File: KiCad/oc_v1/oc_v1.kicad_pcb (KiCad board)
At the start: 2 copper layers, 20 parts, among them J1 ESC_CTRL, J10 STPR_CTRL, J11 ENC_A, J12 ENC_A, J13 MOTOR, J14 Screw_Terminal_01x02, J2 ESC_SEN, J3 BLDC_SEN, J4 ESC_CTRL, J5 ESC_SEN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

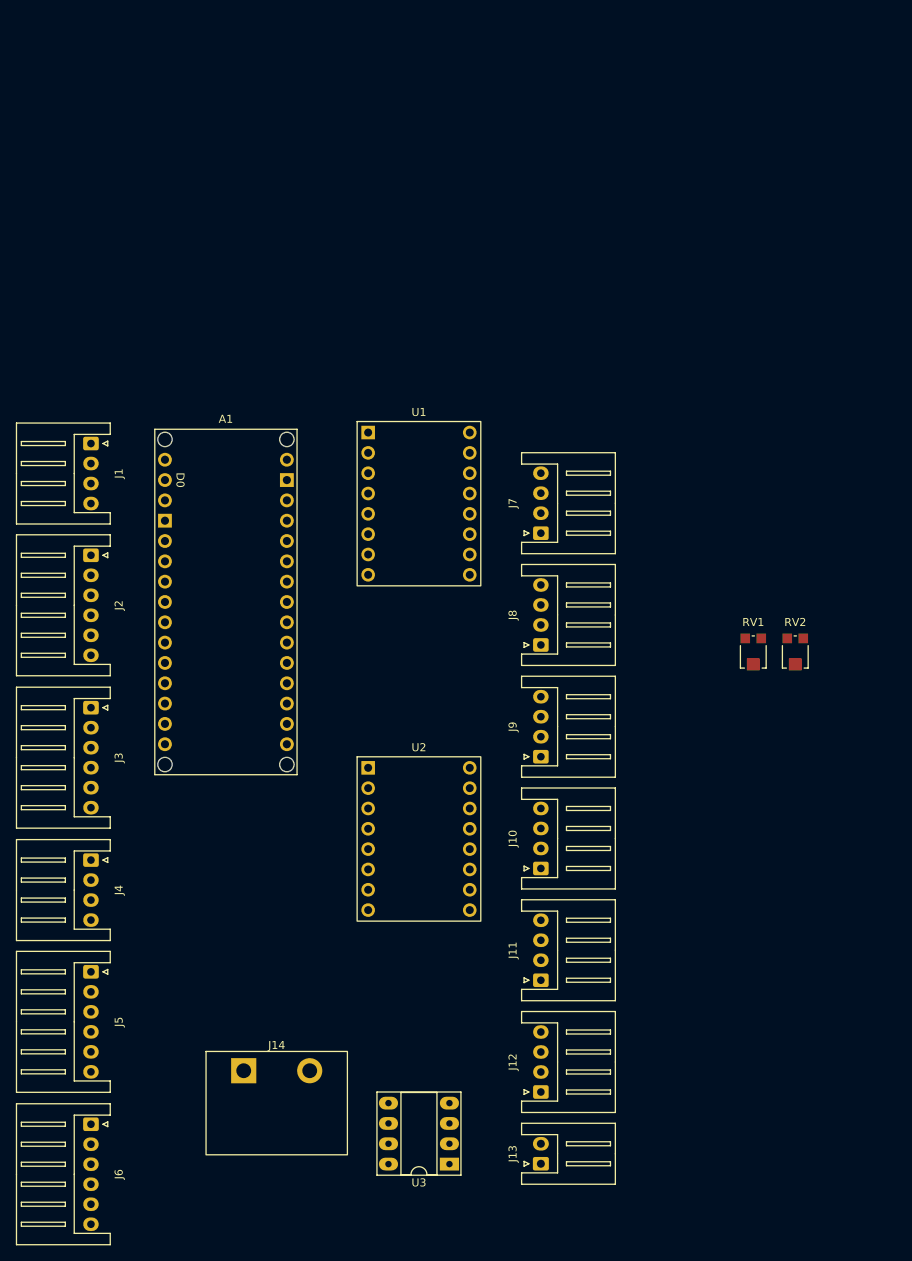
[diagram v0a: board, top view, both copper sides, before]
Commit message: Completed onboard controller PCB
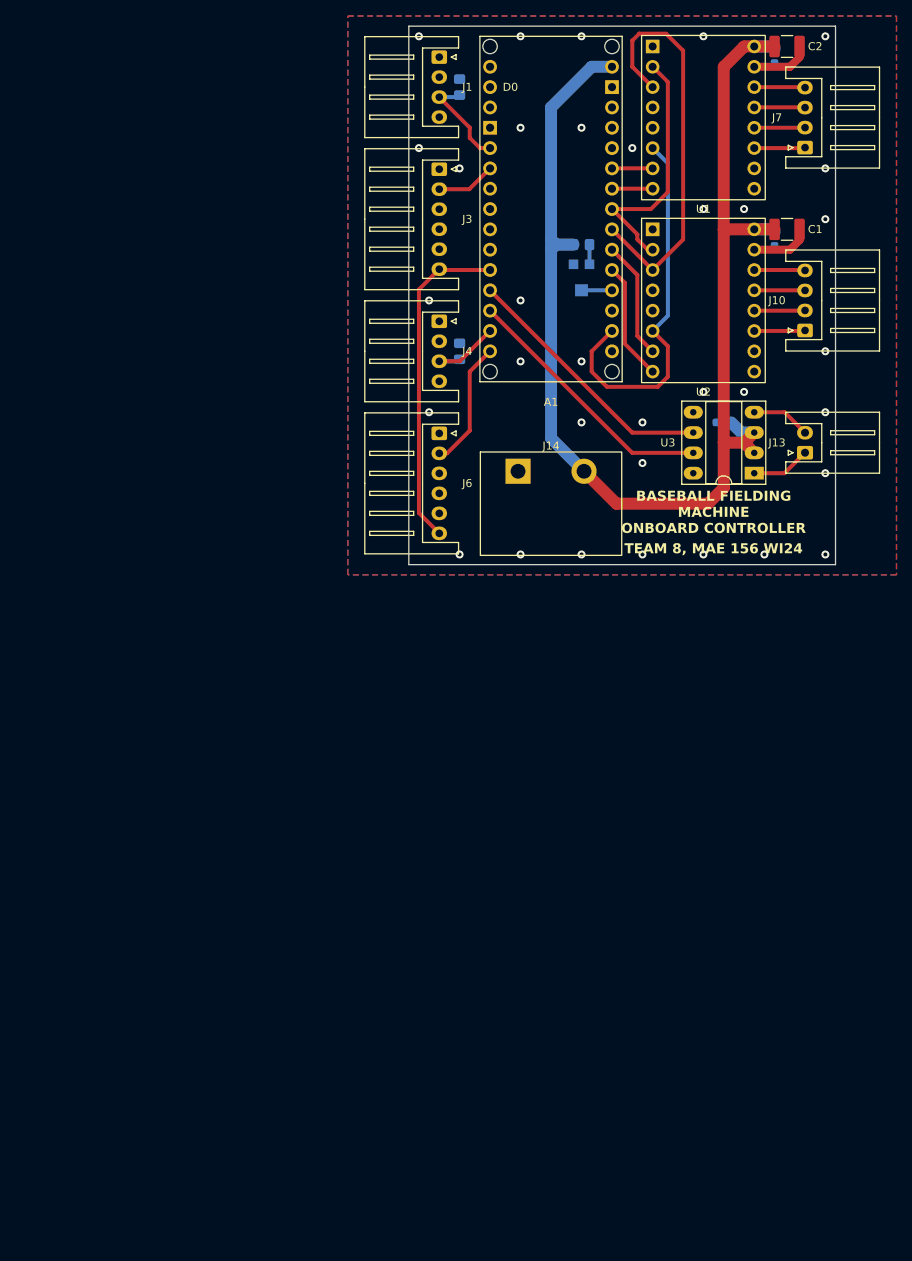
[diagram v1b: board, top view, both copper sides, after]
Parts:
- removed J11, J12, J8, J9: ENC_A, Connector_JST:JST_XH_S4B-XH-A_1x04_P2.50mm_Horizontal
- removed J2, J5: ESC_SEN, Connector_JST:JST_XH_S6B-XH-A_1x06_P2.50mm_Horizontal
- removed RV2: R_Potentiometer_Trim, Footprint Library:Bourns_TC33X_Potentiometer
- added C1: 100u, Capacitor_SMD:C_1210_3225Metric_Pad1.33x2.70mm_HandSolder, F.Cu at (160.3, 72.4)
- added C2: 100u, Capacitor_SMD:C_1210_3225Metric_Pad1.33x2.70mm_HandSolder, F.Cu at (160.3, 49.5)
- added C3: 0.1u, Capacitor_SMD:C_0603_1608Metric_Pad1.08x0.95mm_HandSolder, B.Cu at (158.8, 50.8)
- added C4: 0.1u, Capacitor_SMD:C_0603_1608Metric_Pad1.08x0.95mm_HandSolder, B.Cu at (158.8, 73.7)
- added C5: 0.1u, Capacitor_SMD:C_0603_1608Metric_Pad1.08x0.95mm_HandSolder, B.Cu at (152.4, 96.5)
- added R1: 10k, Resistor_SMD:R_0805_2012Metric_Pad1.20x1.40mm_HandSolder, B.Cu at (119.4, 54.6)
- added R2: 10k, Resistor_SMD:R_0805_2012Metric_Pad1.20x1.40mm_HandSolder, B.Cu at (119.4, 87.6)
- added R3: 10k, Resistor_SMD:R_0805_2012Metric_Pad1.20x1.40mm_HandSolder, B.Cu at (134.6, 74.3)
- RV1: moved to B.Cu
- moved J6 96.7 mm to (116.8, 97.9)
- moved J13 94.8 mm to (162.6, 100.3)
- moved U3 94.4 mm to (156.2, 102.9)
- moved J14 82.4 mm to (126.7, 102.6)
- moved J4 80.2 mm to (116.8, 83.9)
- moved J3 80.2 mm to (116.8, 64.9)
- moved U2 76.1 mm to (143.5, 72.4)
- moved J10 74.9 mm to (162.6, 85.0)
- moved J1 65.0 mm to (116.8, 50.9)
- moved A1 63.8 mm to (130.8, 91.4)
- moved U1 59.9 mm to (143.5, 49.5)
- moved J7 58.4 mm to (162.6, 62.2)
- moved RV1 51.5 mm to (134.6, 78.6), turned to 180 degrees
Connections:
- A1 pad A1: /FOR -> /DIR2
- A1 pad A2: /BACK -> /STEP2
- A1 pad A3: /EZ+2 -> /MS2
- A1 pad A4: /EZ+1 -> /MS1
- A1 pad A5: unconnected-(A1-A5/SCL-PadA5) -> /DIR1
- A1 pad A6: unconnected-(A1-PadA6) -> /STEP1
- A1 pad D10: /STEP2 -> /FOR
- A1 pad D11: /DIR2 -> /SERVO2
- A1 pad D12: /EA+2 -> /HALL2
- A1 pad D13: /EB+2 -> unconnected-(A1-D13_SCK-PadD13)
- A1 pad D4: /SERVO2 -> unconnected-(A1-PadD4)
- A1 pad D5: /HALL2 -> unconnected-(A1-PadD5)
- A1 pad D6: /STEP1 -> unconnected-(A1-PadD6)
- A1 pad D7: /DIR1 -> unconnected-(A1-PadD7)
- A1 pad D8: /EA+1 -> /3V3
- A1 pad D9: /EB+1 -> /BACK
- J14 pad 1: +12V -> GND
- J14 pad 2: GND -> +12V
- J3 pad 3: Net-(J2-Pin_3) -> unconnected-(J3-Pin_3-Pad3)
- J3 pad 4: Net-(J2-Pin_4) -> unconnected-(J3-Pin_4-Pad4)
- J3 pad 5: Net-(J2-Pin_5) -> unconnected-(J3-Pin_5-Pad5)
- J3 pad 6: +3V3 -> /3V3
- J6 pad 3: Net-(J5-Pin_3) -> unconnected-(J6-Pin_3-Pad3)
- J6 pad 4: Net-(J5-Pin_4) -> unconnected-(J6-Pin_4-Pad4)
- J6 pad 5: Net-(J5-Pin_5) -> unconnected-(J6-Pin_5-Pad5)
- J6 pad 6: +3V3 -> /3V3
- RV1 pad 1: +12V -> Net-(R3-Pad2)
- RV1 pad 2: unconnected-(RV1-Pad2) -> Net-(A1-PadA0)
- RV1 pad 3: Net-(RV1-Pad3) -> GND
- U1 pad 2: unconnected-(U1-MS1-Pad2) -> /MS1
- U1 pad 3: unconnected-(U1-MS2-Pad3) -> /MS2
- U2 pad 2: unconnected-(U2-MS1-Pad2) -> /MS1
- U2 pad 3: unconnected-(U2-MS2-Pad3) -> /MS2
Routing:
- net +12V: track 0.00 -> 162.1 mm
- net /MS2: track 0.00 -> 50.6 mm
- net +3V3: track 0.00 -> 47.9 mm
- net /3V3: track 0.00 -> 41.5 mm
- net /FOR: track 0.00 -> 32.8 mm
- net /BACK: track 0.00 -> 32.8 mm
- net /MS1: track 0.00 -> 31.9 mm
- net /HALL2: track 0.00 -> 16.0 mm
- net GND: track 0.00 -> 15.0 mm, vias 0 -> 34
- net /DIR2: track 0.00 -> 14.8 mm
- net /STEP2: track 0.00 -> 14.8 mm
- net /SERVO1: track 0.00 -> 12.4 mm
- net /SERVO2: track 0.00 -> 10.6 mm
- net /HALL1: track 0.00 -> 7.43 mm
- net Net-(J13-Pin_2): track 0.00 -> 7.41 mm
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- added copper zone on B.Cu, net GND
- added copper zone on F.Cu, net GND
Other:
- board outline added: 53.3 x 67.3 mm
- board text added: "BASEBALL FIELDING MACHINE ONBOARD CONTROLLER"
- board text added: "D.H.L REV. 0 02/22/2024"
- board text added: "TEAM 8, MAE 156 WI24"

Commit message: fixed problem with pcb
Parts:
- moved J14 8.25 mm to (134.9, 102.6), turned to 180 degrees
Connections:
- A1 pad D8: /3V3 -> +3V3
- J14 pad 1: GND -> +12V
- J14 pad 2: +12V -> GND
- J3 pad 6: /3V3 -> +3V3
- J6 pad 6: /3V3 -> +3V3
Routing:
- net +3V3: track 47.9 -> 107.8 mm
- net /3V3: track 41.5 -> 0.00 mm

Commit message: revised onboard pcb
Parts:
- removed C5: 0.1u, Capacitor_SMD:C_0603_1608Metric_Pad1.08x0.95mm_HandSolder
- added D1: D_Zener, Diode_SMD:D_TUMD2, B.Cu at (139.7, 102.9)
- added D2: D_Zener, Diode_SMD:D_TUMD2, B.Cu at (160.7, 73.0)
- added D3: D_Zener, Diode_SMD:D_TUMD2, B.Cu at (160.7, 50.2)
- added D4: D_Zener, Diode_SMD:D_TUMD2, B.Cu at (135.3, 53.3)
- C1: footprint Capacitor_SMD:C_1210_3225Metric_Pad1.33x2.70mm_HandSolder -> Capacitor_THT:CP_Radial_D5.0mm_P2.50mm
- C2: value 100u -> 0.1u; footprint Capacitor_SMD:C_1210_3225Metric_Pad1.33x2.70mm_HandSolder -> Capacitor_SMD:C_0603_1608Metric_Pad1.08x0.95mm_HandSolder; moved to B.Cu
- moved C1 40.6 mm to (127.0, 95.6), turned to -90 degrees
- moved C2 23.8 mm to (158.8, 73.3), turned to -90 degrees
- moved C4 23.3 mm to (154.3, 96.5), turned to 180 degrees
- moved J14 8.96 mm to (143.8, 103.7)
- moved U3 1.90 mm to (158.1, 102.9)
- moved J10 0.64 mm to (162.6, 84.4)
- moved J7 0.64 mm to (162.6, 61.5)
- moved C3 0.41 mm to (158.8, 50.4)
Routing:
- net GND: track 15.0 -> 0.00 mm, vias 34 -> 30
- net +12V: track 162.1 -> 164.3 mm
- net Net-(J13-Pin_1): track 7.41 -> 5.51 mm
- net /FOR: track 32.8 -> 34.7 mm
- net /BACK: track 32.8 -> 34.7 mm
- net Net-(J13-Pin_2): track 7.41 -> 5.52 mm
- net +3V3: track 107.8 -> 108.4 mm
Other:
- board text added: "D.H.L REV. 1 04/11/2024"
- board text removed: "D.H.L REV. 0 02/22/2024"
